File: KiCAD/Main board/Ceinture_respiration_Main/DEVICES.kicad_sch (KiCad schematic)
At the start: 20 parts, among them J8 Oled, J9 MEM2061-01-188-00-A_REVA, M1 Motor_DC, Q1 MMBT3904, SW1 SW_Push, SW2 SW_Push, SW3 SW_Push, SW4 SW_Push, U1 DRV2605LDGS

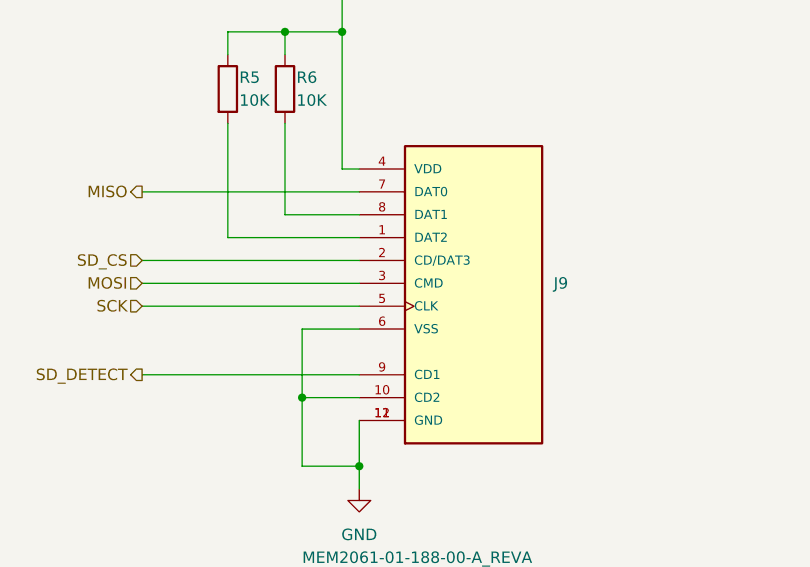
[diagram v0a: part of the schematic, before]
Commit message: modifié info Part number du main board pour faciliter la génération de BOM non JLC
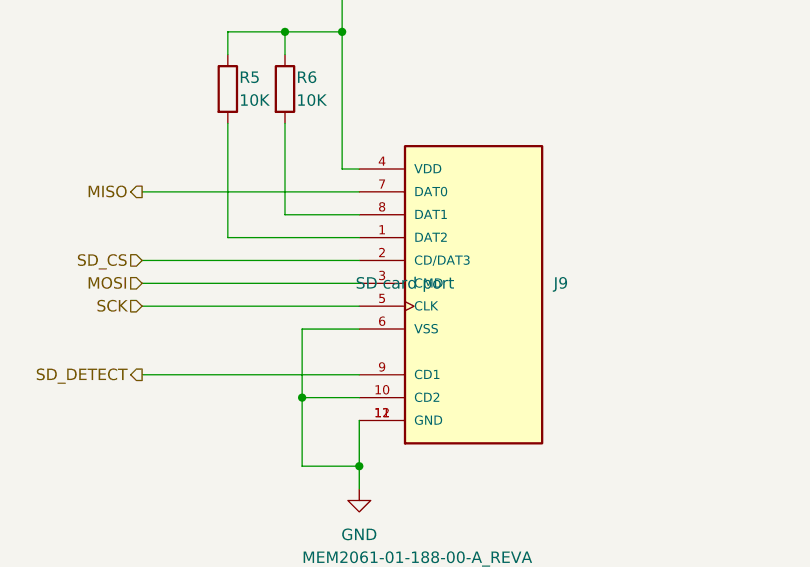
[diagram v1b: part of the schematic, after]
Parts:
- D1: LCSC (none) -> C779429
- D2: LCSC (none) -> C2895476
- J8: Digikey (none) -> AOM12864A0-0.96WW-ANO; MPN -- -> AOM12864A0-0.96WW-ANO / ER-OLEDM0.96-1B-SPI-I2C; buydisplay.com (none) -> ER-OLEDM0.96-1B-SPI-I2C
- J9: LCSC (none) -> C5151738; MPN (none) -> MEM2061-01-188-00-A_REVA
- M1: MPN (none) -> VC0720B001F
- SW1, SW2, SW3, SW4: LCSC (none) -> C2886900
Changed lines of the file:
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@@
+			)
+		)
+		(property "LCSC" "C2895476"
+			(at 99.3775 43.18 0)
+			(effects
+				(font
+					(size 1.27 1.27)
+				)
+				(hide yes)
 			)
 		)
@@
 			)
 		)
+		(property "LCSC" "C2886900"
+			(at 40.64 44.45 0)
+			(effects
+				(font
+					(size 1.27 1.27)
+				)
+				(hide yes)
+			)
+		)
 		(pin "1"
 		)
@@
 			)
 		)
-		(property "MPN" "--"
+		(property "MPN" "AOM12864A0-0.96WW-ANO /  ER-OLEDM0.96-1B-SPI-I2C"
+			(at 58.42 124.46 0)
+			(effects
+				(font
+					(size 1.27 1.27)
+				)
+				(hide yes)
+			)
+		)
+		(property "Digikey" "AOM12864A0-0.96WW-ANO"
+			(at 58.42 124.46 0)
+			(effects
+				(font
+					(size 1.27 1.27)
+				)
+				(hide yes)
+			)
+		)
+		(property "buydisplay.com" "ER-OLEDM0.96-1B-SPI-I2C"
 			(at 58.42 124.46 0)
 			(effects
@@
 			)
 		)
+		(property "LCSC" "C2886900"
+			(at 40.64 30.48 0)
+			(effects
+				(font
+					(size 1.27 1.27)
+				)
+				(hide yes)
+			)
+		)
 		(pin "1"
 		)
@@
 			)
 		)
-		(property "Description" ""
+		(property "Description" "SD card port"
 			(at 147.955 137.16 0)
 			(effects
@@
 			)
 		)
+		(property "LCSC" "C5151738"
+			(at 164.465 137.16 0)
+			(effects
+				(font
+					(size 1.27 1.27)
+				)
+				(hide yes)
+			)
+		)
+		(property "MPN" "MEM2061-01-188-00-A_REVA"
+			(at 147.955 137.16 0)
+			(effects
+				(font
+					(size 1.27 1.27)
+				)
+				(hide yes)
+			)
+		)
 		(pin "1"
 		)
@@
 					(size 1.27 1.27)
 				)
+			)
+		)
+		(property "LCSC" "C2886900"
+			(at 40.64 69.215 0)
+			(effects
+				(font
+					(size 1.27 1.27)
+				)
+				(hide yes)
 			)
 		)
@@
 			)
 		)
+		(property "LCSC" "C779429"
+			(at 99.3775 31.75 0)
+			(effects
+				(font
+					(size 1.27 1.27)
+				)
+				(hide yes)
+			)
+		)
 		(pin "1"
 		)
@@
 		)
 		(property "LCSC" ""
+			(at 257.81 54.61 0)
+			(effects
+				(font
+					(size 1.27 1.27)
+				)
+				(hide yes)
+			)
+		)
+		(property "MPN" "VC0720B001F"
 			(at 257.81 54.61 0)
 			(effects
@@
 			)
 		)
+		(property "LCSC" "C2886900"
+			(at 40.64 57.785 0)
+			(effects
+				(font
+					(size 1.27 1.27)
+				)
+				(hide yes)
+			)
+		)

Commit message: Changé # pièce switch sur main board poru utiliser pièces en stock.
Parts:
- SW1, SW2, SW3, SW4: LCSC C2886900 -> C2939211
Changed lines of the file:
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@@
 			)
 		)
-		(property "LCSC" "C2886900"
+		(property "LCSC" "C2939211"
 			(at 40.64 44.45 0)
 			(effects
@@
 			)
 		)
-		(property "LCSC" "C2886900"
+		(property "LCSC" "C2939211"
 			(at 40.64 30.48 0)
 			(effects
@@
 			)
 		)
-		(property "LCSC" "C2886900"
+		(property "LCSC" "C2939211"
 			(at 40.64 69.215 0)
 			(effects
@@
 			)
 		)
-		(property "LCSC" "C2886900"
+		(property "LCSC" "C2939211"
 			(at 40.64 57.785 0)
 			(effects
